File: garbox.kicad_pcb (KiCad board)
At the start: 4 copper layers, 78.7 x 147.3 mm, 87 parts, among them J1 Batteries Terminal, J2 USB_Header, J3 USB4056-03-A_REVA2, J4 MSD-4-A, J5 SD_Header, J6 PowerBreakoutHeader, J7 BMS_Header, J8 Audio_Header, J9 GPIO_Header, U1 ESP32-S3-WROOM-1-N4R8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

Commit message: fixed usb clearance, added ground plane to top and bottom
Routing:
- net +5V: track 95.2 -> 100.5 mm
- net /ChargeStatus: track 87.1 -> 87.7 mm
- added copper zone on B.Cu, net GND
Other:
- outline, holes or cut-outs redrawn
- board text added: "usb c male"

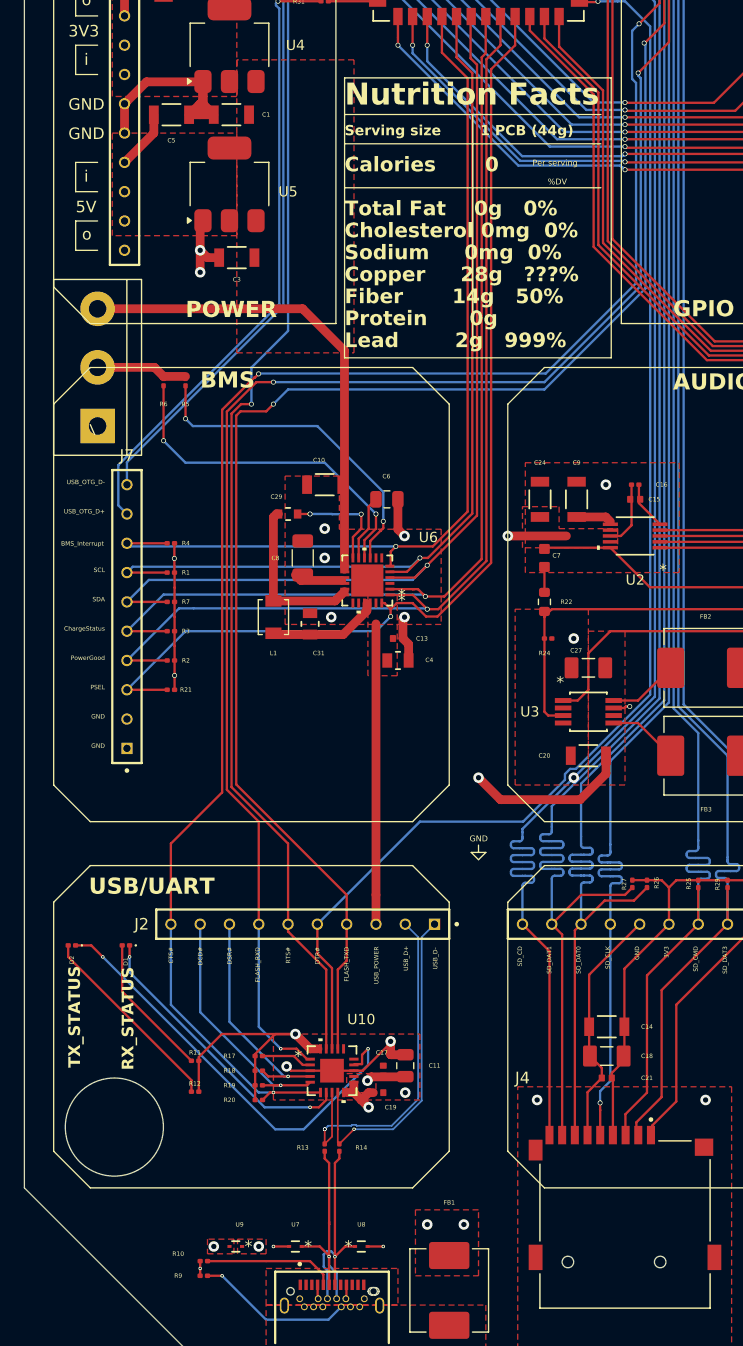
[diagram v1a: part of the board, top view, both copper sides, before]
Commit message: designated MPN parts from JLC library
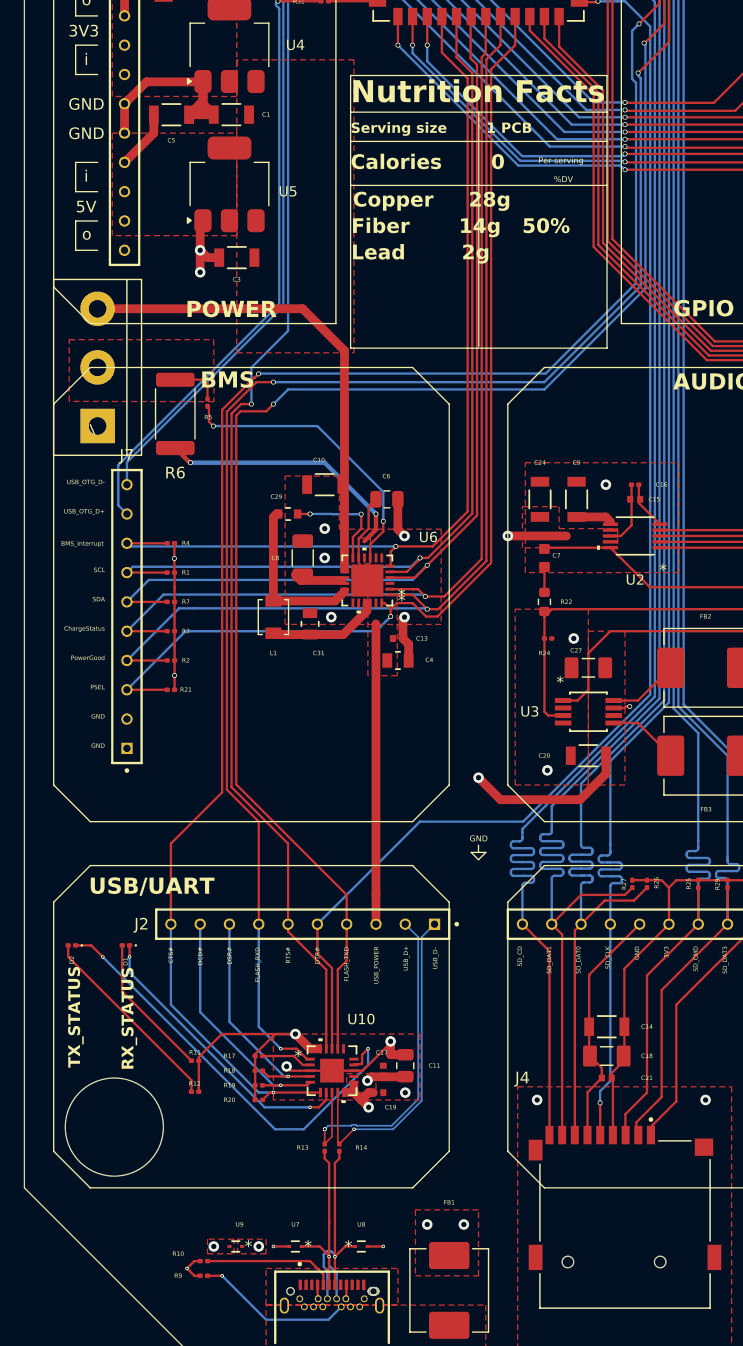
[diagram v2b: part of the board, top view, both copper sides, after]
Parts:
- R6: footprint Resistor_SMD:R_0201_0603Metric -> Resistor_SMD:R_2512_6332Metric
- moved R6 2.93 mm to (89.3, 92.9)
- moved R5 2.61 mm to (92.1, 91.9)
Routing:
- net Net-(U6-CBSET): track 30.0 -> 22.5 mm
- net /BatteryManagement/PackMid: track 7.95 -> 4.26 mm
- net Net-(U6-MID): track 28.8 -> 25.2 mm
- net GND: track 109.4 -> 110.9 mm
- added copper zone on F.Cu, net /BatteryManagement/PackMid
- added copper zone on F.Cu, net Net-(U6-CBSET)
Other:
- rule pad_to_mask_clearance: 0 -> 0.0508
- board text added: "Copper 28g"
- board text added: "Lead 2g"
- board text added: "Serving size 1 PCB"
- board text removed: "Cholesterol 0mg 0%"
- board text removed: "Copper 28g ???%"
- board text removed: "Lead 2g 999%"
- board text removed: "Protein 0g"
- board text removed: "Serving size 1 PCB (44g)"
- board text removed: "Sodium 0mg 0%"
- board text removed: "Total Fat 0g 0%"

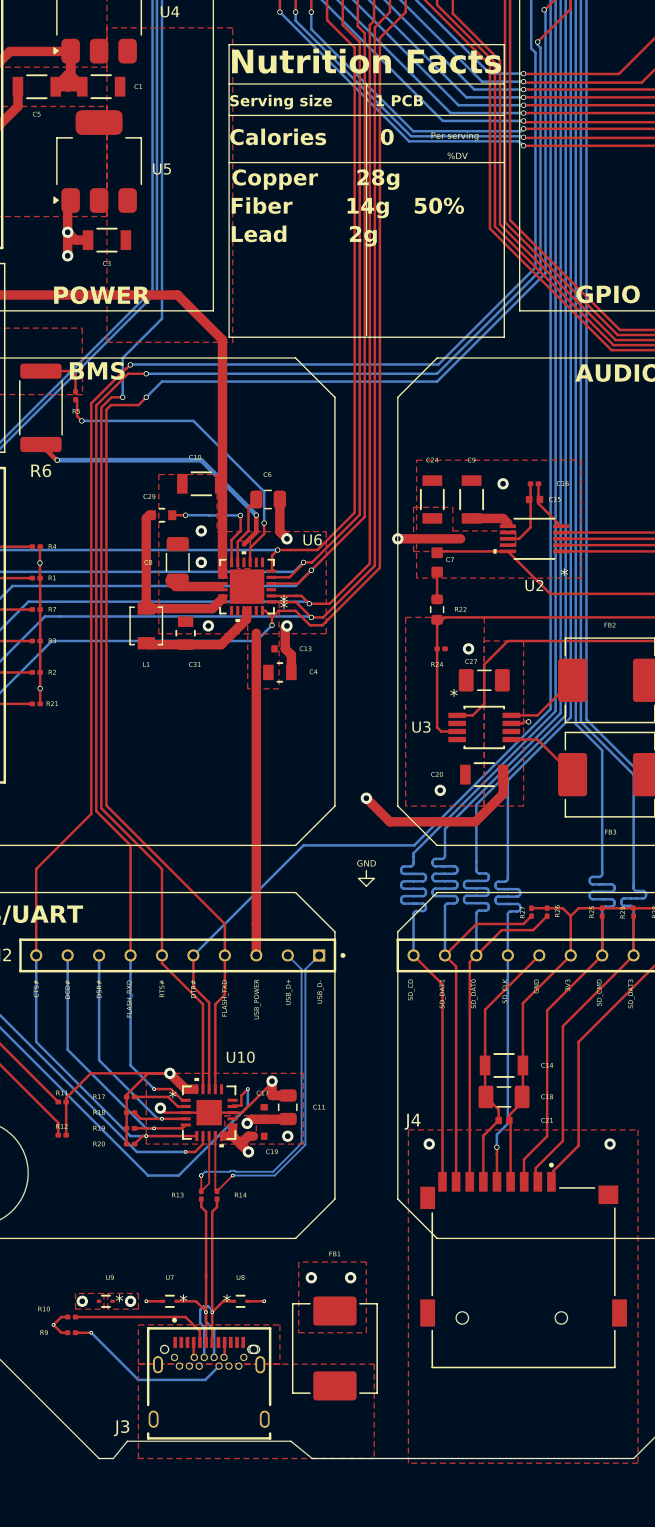
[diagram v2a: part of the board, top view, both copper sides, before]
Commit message: Updated part numbers
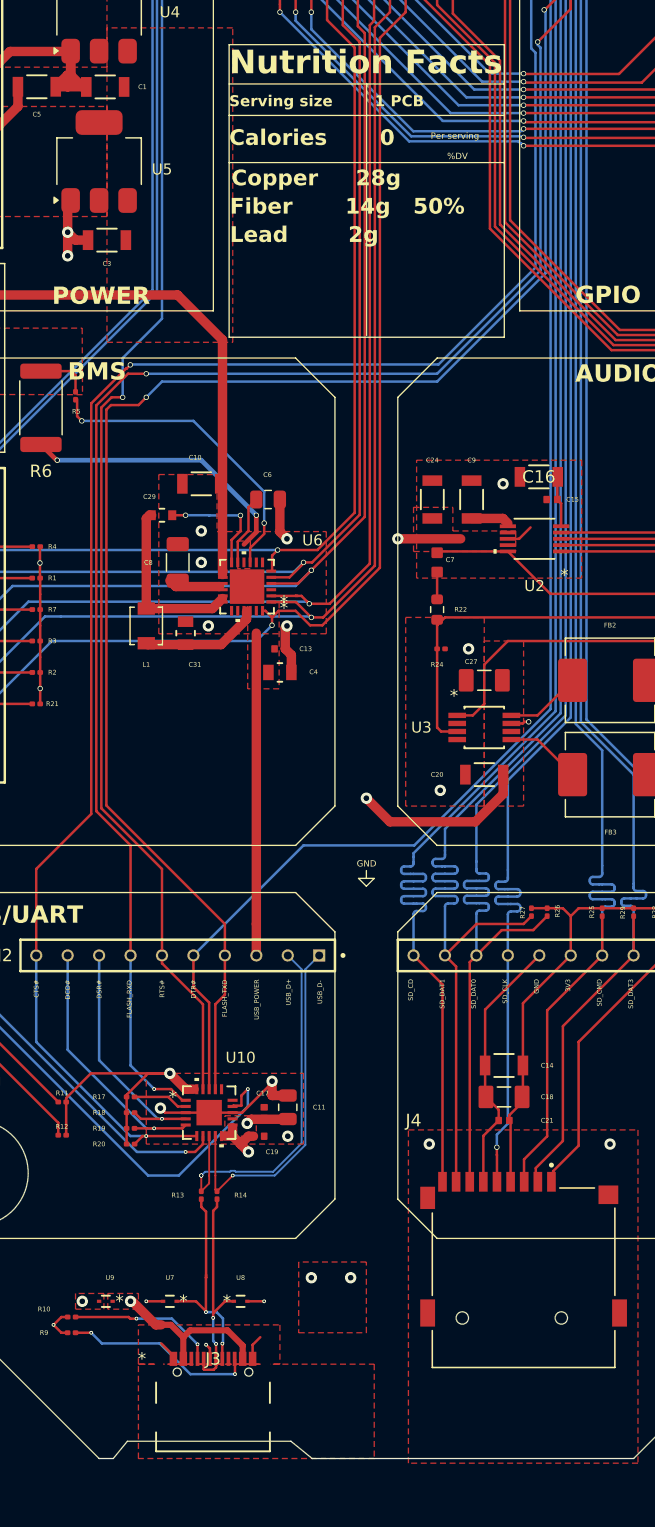
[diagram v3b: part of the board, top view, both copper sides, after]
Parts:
- removed FB1: GZ1608D601TF, Inductor_SMD:L_Sunlord_MWSA0603S
- C16: footprint Capacitor_SMD:C_0201_0603Metric -> CL31A106KBHNNNE:CAP_CL31_SAM
- D1: value RX_STATUS_LED -> LED
- D2: value TX_STATUS_LED -> LED
- D3, D4: value GP_LED -> LED
- J2: value USB_Header -> TS-110-G-A
- J3: footprint USB4056_03_A:GCT_USB4056-03-A_REVA2 -> 12402012E212A:12402012E212A_AMP
- J5: value SD_Header -> TS-110-G-A
- J6: value PowerBreakoutHeader -> TS-110-G-A
- J7: value BMS_Header -> TS-110-G-A
- J8: value Audio_Header -> TS-110-G-A
- J9: value GPIO_Header -> TS-110-G-A
- moved C15 1.42 mm to (130.6, 100.3)
- moved J3 1.24 mm to (103.2, 173.4)
- moved C16 0.66 mm to (129.5, 98.5)
- moved C1 0.33 mm to (94.5, 67.0)
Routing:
- net /USB_PowerSupply: track 73.3 -> 84.9 mm
- net Net-(J3-CC1-PadB5): track 13.6 -> 15.5 mm, vias 1 -> 2
- net Net-(J3-D--PadA7): track 19.2 -> 17.8 mm, vias 1 -> 2
- net Net-(J3-CC1-PadA5): track 11.4 -> 11.9 mm, vias 0 -> 2
- net Net-(J3-D+-PadA6): track 18.8 -> 18.4 mm, vias 1 -> 3

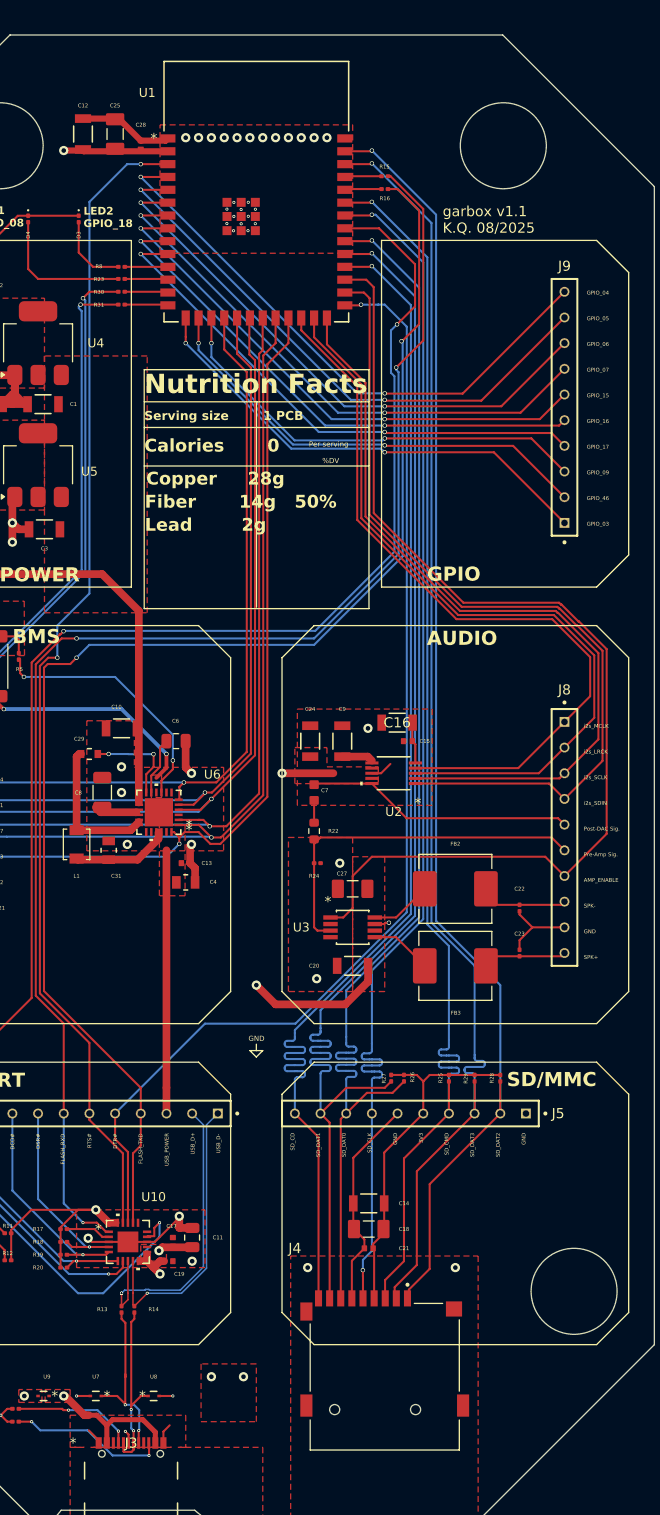
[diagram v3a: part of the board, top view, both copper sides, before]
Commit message: swapped esp32-s3-wroom-1-n4r8 for esp32-s3-wroom-1u-n4r8 board, fixed unconnected net on USB connector, and tidied up some traces on usb.
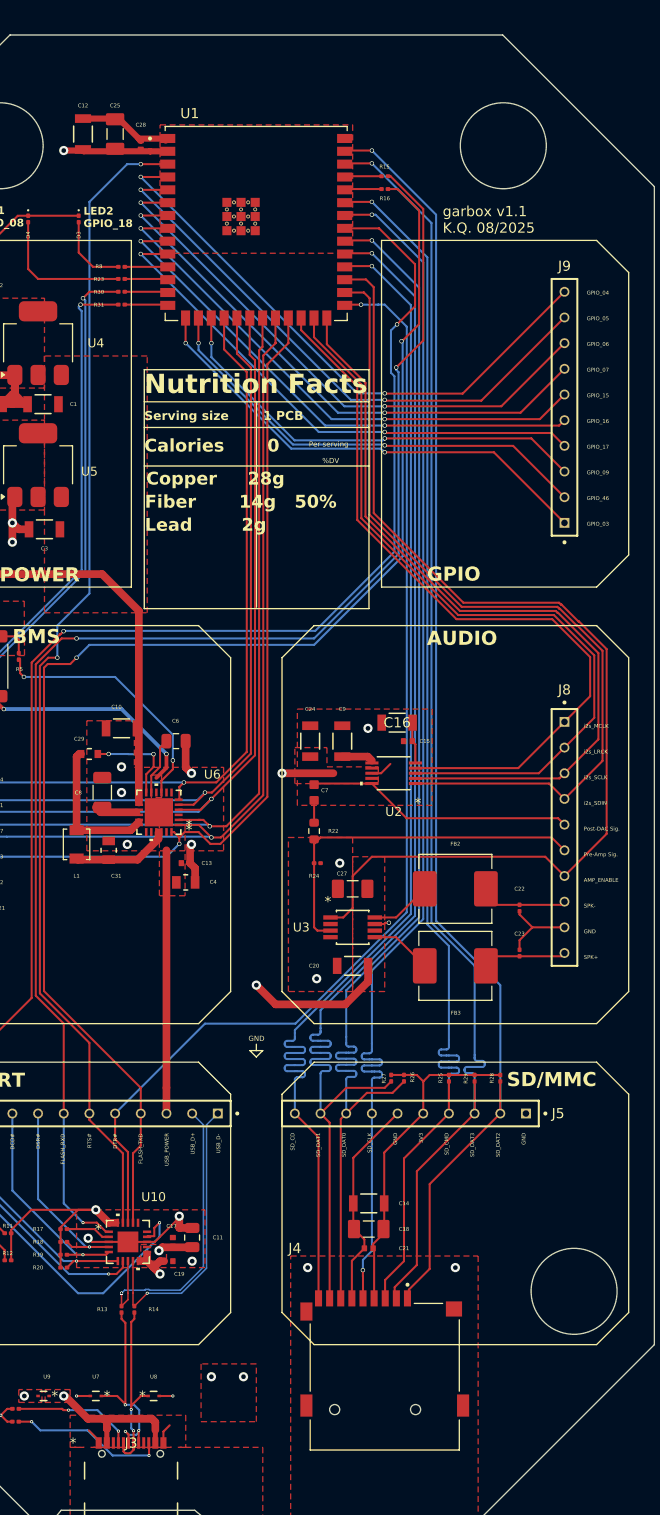
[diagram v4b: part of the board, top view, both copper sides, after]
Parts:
- U1: value ESP32-S3-WROOM-1-N4R8 -> ESP32-S3-WROOM-1U-N4R8; footprint ESP32_S3_WROOM_1_N4R8:ESP32-S3-WROOM-1_EXP -> ESP32_S3_WROOM_1U_N4R8:XCVR_ESP32-S3-WROOM-1U-N4R8
- moved U1 3.15 mm to (115.6, 49.1)
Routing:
- net Net-(J3-D+-PadA6): track 18.4 -> 19.9 mm
- net /USB_PowerSupply: track 84.9 -> 86.1 mm
- net GND: track 111.0 -> 111.7 mm, vias 47 -> 23
- added copper zone on F.Cu, net (none)
- removed copper zone on F.Cu, net Net-(J3-SHELL_GND)

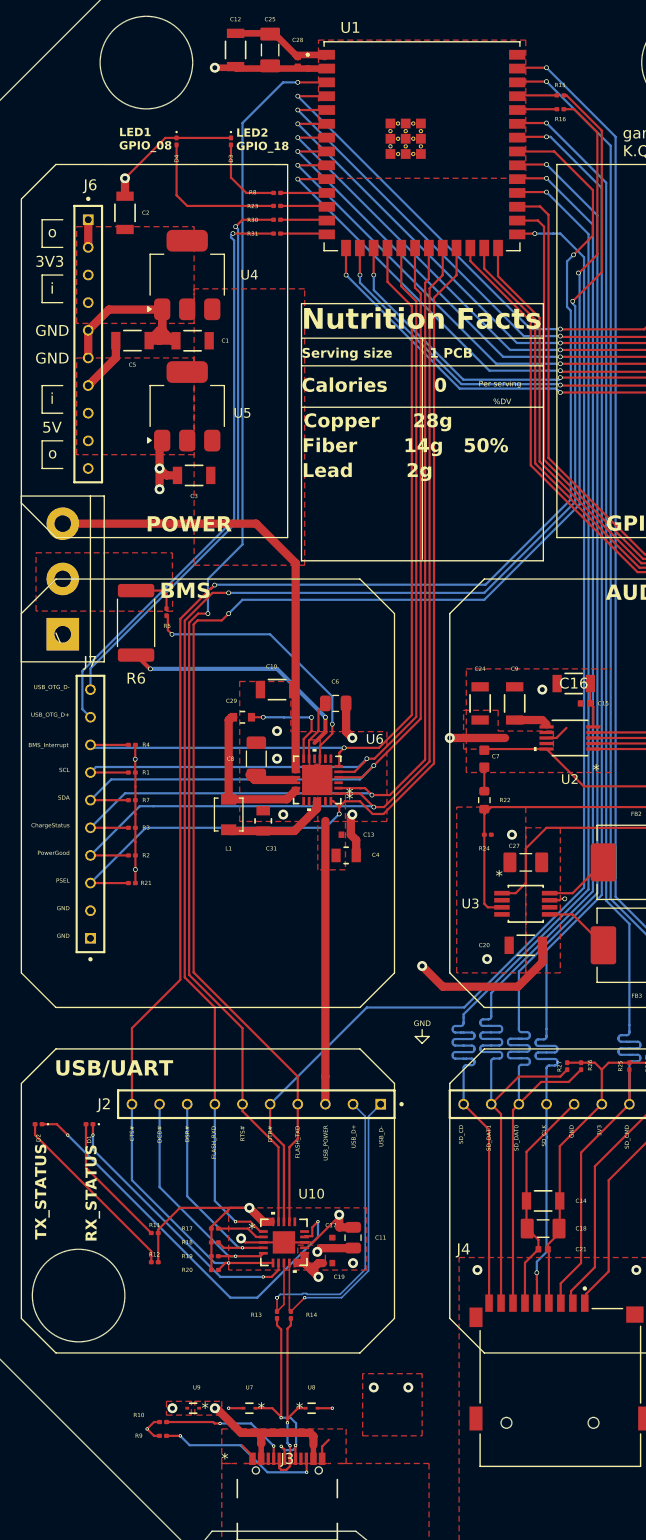
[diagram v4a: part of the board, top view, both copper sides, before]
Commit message: changed minimum hole/diameter size to 0.2mm/0.45mm for manufacturer compliance. moved some traces around to avoid DRC errors accordingly
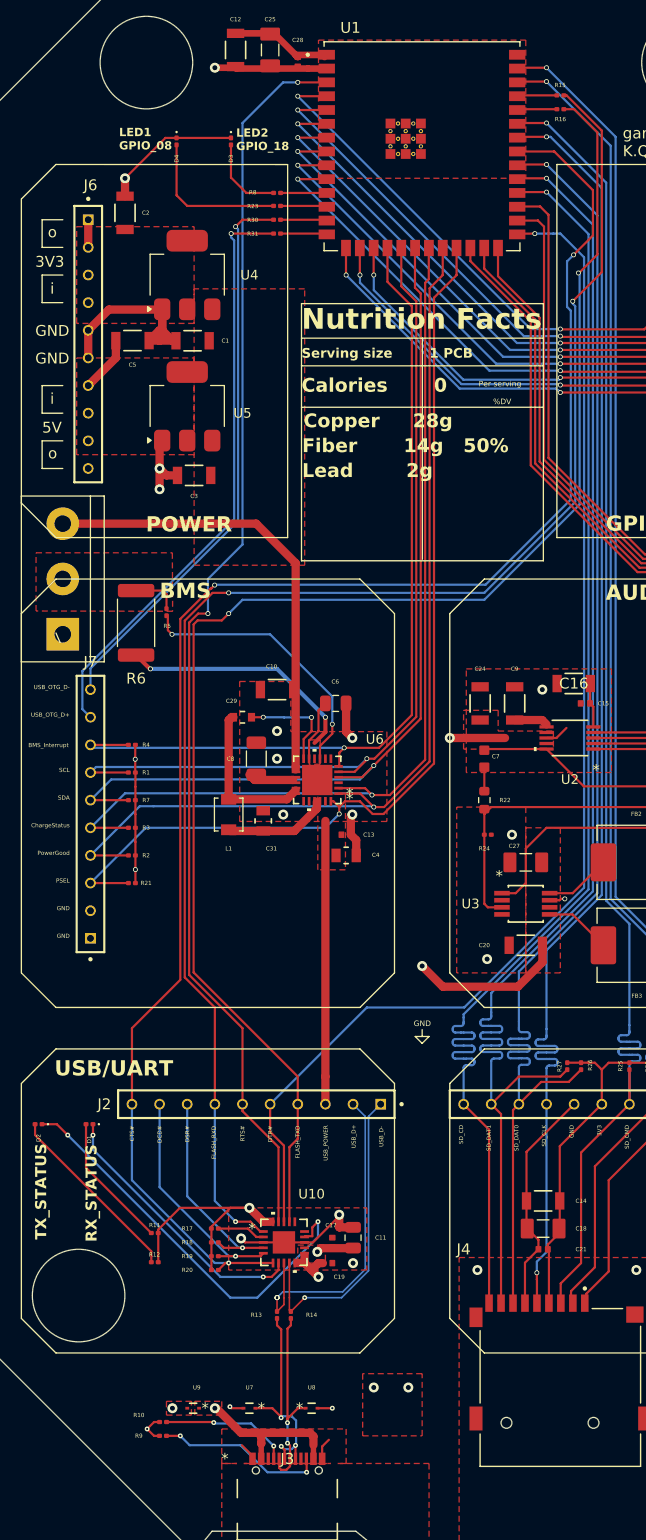
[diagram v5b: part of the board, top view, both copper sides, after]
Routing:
- net /USB_PowerSupply: track 86.1 -> 85.4 mm
